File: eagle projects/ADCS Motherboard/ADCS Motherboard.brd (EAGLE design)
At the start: 91 x 91 mm, 141 parts, among them J1 HDR_10_EZFET_DEBUGGER, J11 CNC_3221-10-0300-00, J5 CNC_3221-10-0300-00, J7 TE-1734829-3, Q1 BSR802NL6327HTSA1, U1 MSP430F5529IPN, U10 TSV991AILT, U2 TSV991AILT, U3 ADS7841E_2K5, U4 TSV991AILT, U5 DMC4050SSDQ-13, U7 HMC1053, U9 BMX160, Y1 32.768kHz, Y2 CSTCR4M00G15L99, Y3 32.768kHz

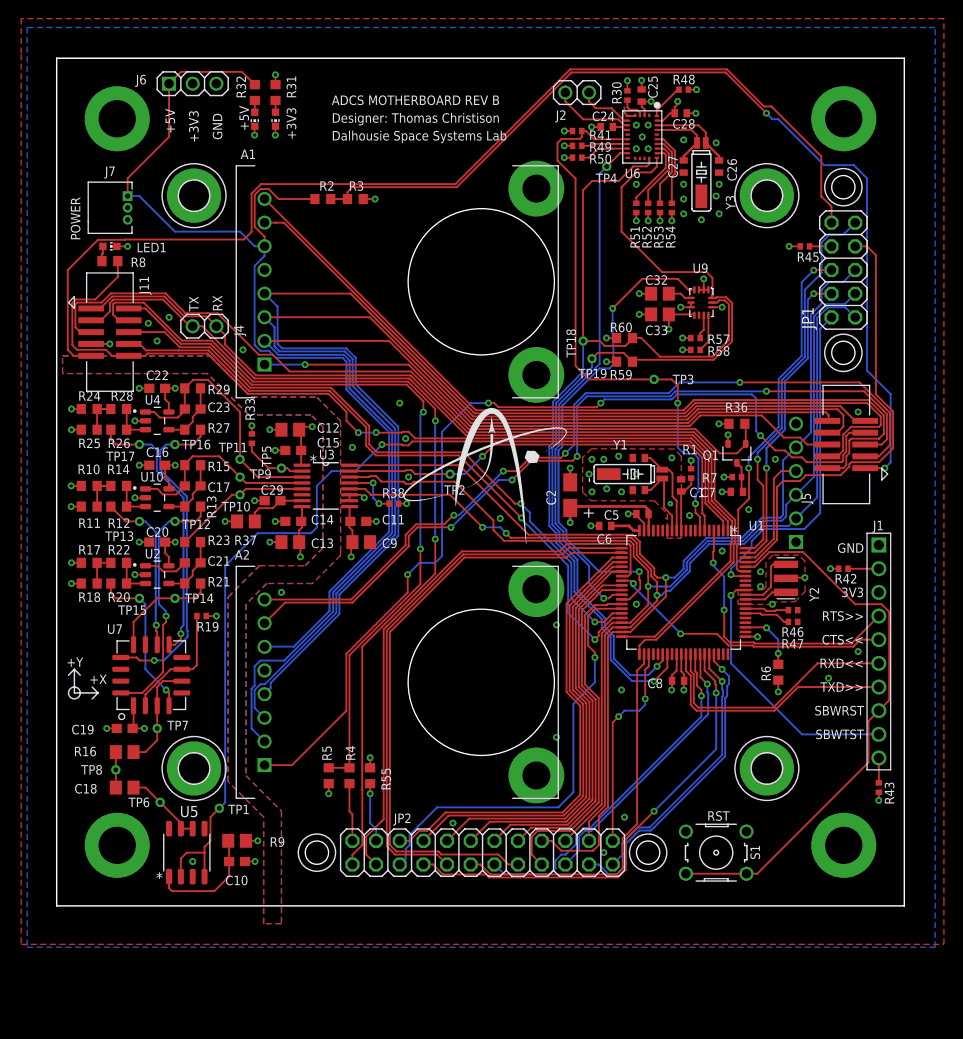
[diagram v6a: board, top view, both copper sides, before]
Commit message: stitching vias and silkscreen and fixed reversed totem pole driver (oops)
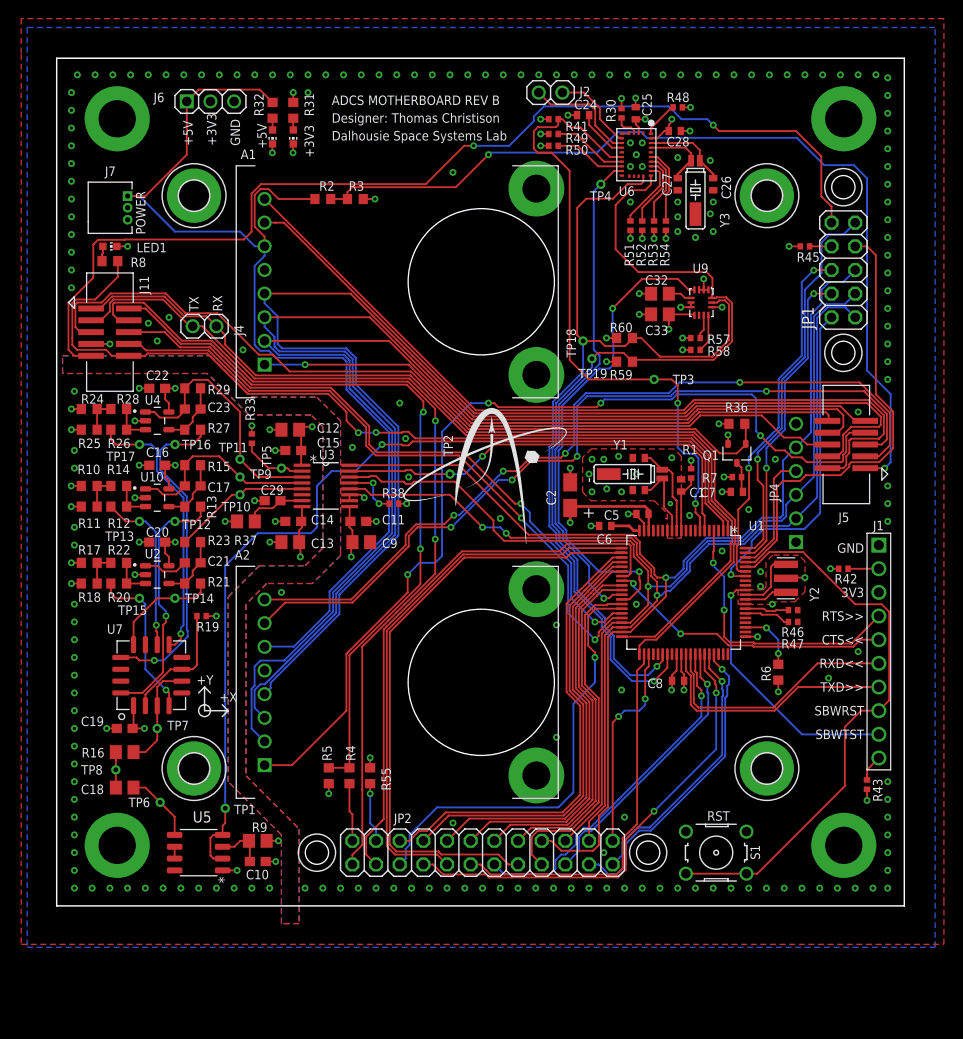
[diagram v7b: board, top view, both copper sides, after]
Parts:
- moved J2 2.86 mm to (53.0, 87.3)
- moved R49 2.84 mm to (53.3, 82.9)
- moved C24 2.84 mm to (56.5, 84.9)
- moved R41 2.84 mm to (53.3, 84.5)
- moved R50 2.84 mm to (53.3, 81.6)
- moved J6 2.69 mm to (16.5, 86.4)
- moved LED2 2.69 mm to (25.4, 82.5)
- moved LED3 2.69 mm to (23.2, 82.5)
- moved R31 2.69 mm to (25.4, 85.4)
- moved R32 2.69 mm to (23.2, 85.4)
- moved C10 2.22 mm to (21.6, 4.76)
- moved R9 2.22 mm to (21.6, 6.99)
- moved C26 2.01 mm to (70.5, 77.5)
- moved C27 2.01 mm to (66.7, 77.5)
- moved C28 2.01 mm to (66.4, 83.2)
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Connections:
- new net N$48: U5.6, U5.7
- net GND: now also U5.1; no longer U5.3
- net N$39: now also U5.3; no longer U5.1
- net N$9: now also U5.5; no longer U5.6, U5.7
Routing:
- net N$39: track 12.3 -> 5.35 mm
- net BNO055_RST: track 63.6 -> 70.0 mm
- net CAM_5V_PRESENT: track 104.7 -> 99.4 mm
- net HMC1053_RESET: track 108.2 -> 103.0 mm
- net N$13: track 1.73 -> 5.57 mm
- net N$17: track 8.71 -> 12.2 mm
- net N$16: track 5.96 -> 9.09 mm
- net Z-_SUN_3V_PRESENT: track 115.0 -> 111.9 mm, vias 0 -> 2
- net N$42: track 5.01 -> 8.06 mm
- net N$43: track 5.33 -> 7.74 mm
- net BNO055_INT: track 55.7 -> 54.1 mm
- net UCB1_I2C_SCL: track 96.4 -> 94.8 mm
- net N$48: track 0.00 -> 1.27 mm
- net RST/SBWTDIO: track 63.8 -> 64.9 mm
- net N$9: track 8.53 -> 7.65 mm
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
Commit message: I thinks its done
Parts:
- added R34, R35, R39: 5.1M, rcl:R0402
- R37: device rcl:R0805 -> rcl:R0603
- R55: device rcl:R0603 -> rcl:R0402
- U6: value (none) -> BNO055
- moved J2 17.9 mm to (70.8, 85.7), turned to 90 degrees
- moved R38 0.63 mm to (36.2, 42.5)
- moved C32 0.32 mm to (64.5, 65.7)
- moved C33 0.32 mm to (64.5, 63.5)
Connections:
- removed net N$2: C32.1, U9.5
- removed net N$41: U1.44
- removed net TB0.3: U1.58
- removed net TB0.4: U1.59
- net !CS!_SUN_Z-: now also U1.3; no longer U1.75
- net +3V3: now also C32.1, U9.5
- net BMX160_INT2: now also R34.2
- net GND: now also R34.1, R35.1, R39.1
- net N$16: now also R35.2
- net N$17: now also R39.2
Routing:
- net GND: track 71.8 -> 84.7 mm, vias 253 -> 311
- net N$16: track 9.09 -> 21.3 mm
- net N$17: track 12.2 -> 21.6 mm
- net RST/SBWTDIO: track 64.9 -> 74.1 mm
- net BMX160_INT2: track 0.00 -> 7.23 mm, vias 0 -> 2
- net Z-_SUN_3V_PRESENT: track 111.9 -> 107.5 mm
- net CAM_5V_PRESENT: track 99.4 -> 95.0 mm
- net +3V3: track 74.2 -> 78.6 mm, vias 25 -> 26
- net !CS!_SUN_Z-: track 38.5 -> 35.1 mm
- net N$2: track 2.57 -> 0.00 mm
- net B_MEAS_X: track 19.8 -> 22.0 mm
- net N$36: track 12.8 -> 14.3 mm
- net BMX160_INT1: track 52.4 -> 53.8 mm
- net CAMERA-2_CS: track 102.9 -> 101.6 mm
- net RW_Y_LOCK: track 67.2 -> 66.3 mm
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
